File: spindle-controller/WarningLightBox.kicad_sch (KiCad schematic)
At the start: 4 parts, among them J22 GX12-4

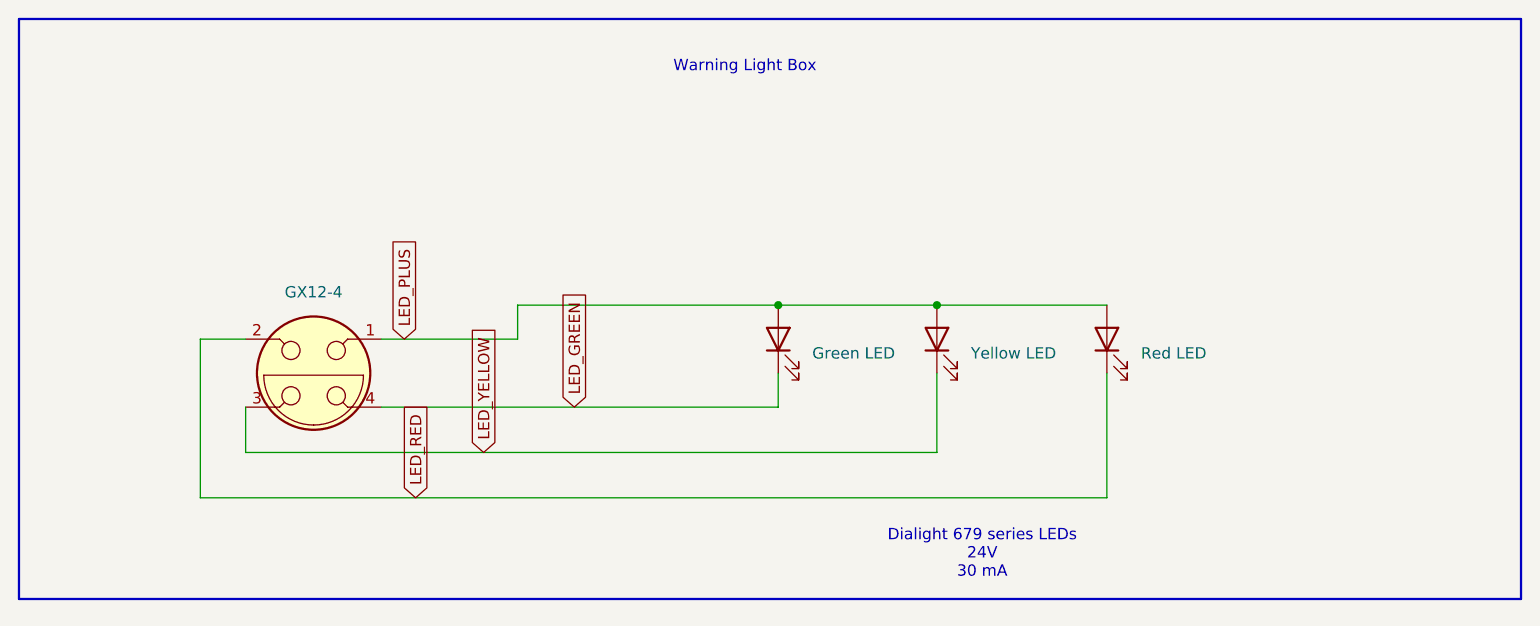
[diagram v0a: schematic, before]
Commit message: Rename project to Spindle_Controller; add VFD_DI1 spindle command path
Renamed CNC_router -> Spindle_Controller for clarity, since this
project is specifically about the spindle controller rather than the
router as a whole. Also adds the GX12-7 cable connector and VFD_DI1
wiring needed to command the spindle on, routes it through a DPDT
safety-interlock switch (SW1) shared with the warning light circuit,
fixes a DAC/ADC signal swap on VFD_VF1/VFD_FM1, and reconciles several
net labels between the root schematic and the VFD Enclosure /
TechnoCNC Controller / Warning Light Box sub-sheets.

Co-Authored-By: Claude Sonnet 5 <noreply@anthropic.com>
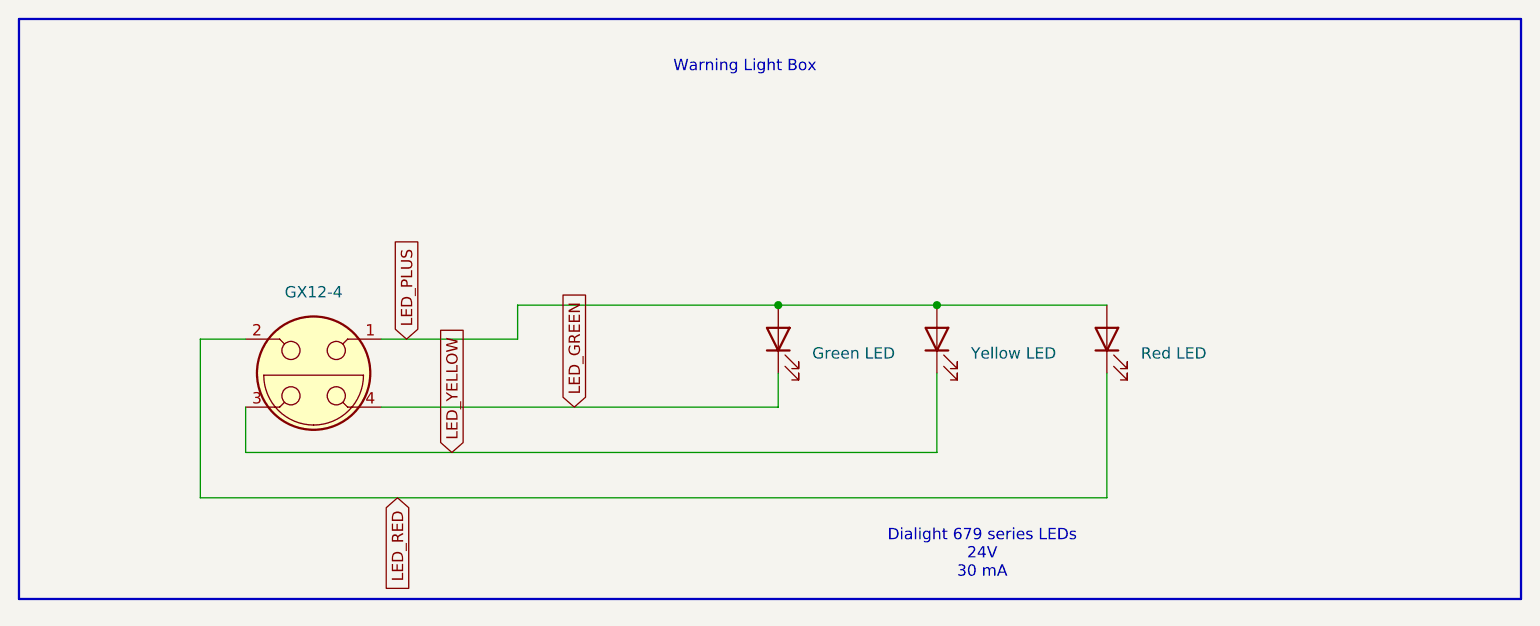
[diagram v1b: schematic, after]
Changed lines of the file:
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@@
 	(global_label "LED_YELLOW"
 		(shape input)
-		(at 78.74 68.58 90)
+		(at 75.184 68.58 90)
 		(fields_autoplaced yes)
 		(effects
@@
 		)
 		(property "Intersheetrefs" "${INTERSHEET_REFS}"
-			(at 78.74 54.1044 90)
+			(at 75.184 54.1044 90)
 			(hide yes)
 			(show_name no)
@@
 	(global_label "LED_PLUS"
 		(shape input)
-		(at 69.85 55.88 90)
+		(at 70.104 55.88 90)
 		(fields_autoplaced yes)
 		(effects
@@
 		)
 		(property "Intersheetrefs" "${INTERSHEET_REFS}"
-			(at 69.85 43.642 90)
+			(at 70.104 43.642 90)
 			(hide yes)
 			(show_name no)
@@
 	(global_label "LED_RED"
 		(shape input)
-		(at 71.12 73.66 90)
+		(at 69.088 73.66 270)
 		(fields_autoplaced yes)
 		(effects
@@
 				(size 1.27 1.27)
 			)
-			(justify left)
+			(justify right)
 		)
 		(property "Intersheetrefs" "${INTERSHEET_REFS}"
-			(at 71.12 62.5711 90)
-			(hide yes)
-			(show_name no)
-			(do_not_autoplace no)
-			(effects
-				(font
-					(size 1.27 1.27)
-				)
-				(justify left)
+			(at 69.088 84.7489 90)
+			(hide yes)
+			(show_name no)
+			(do_not_autoplace no)
+			(effects
+				(font
+					(size 1.27 1.27)
+				)
+				(justify right)
 			)
 		)
@@
 		)
 		(instances
-			(project "CNC_router"
+			(project "Spindle_Controller"
 				(path "/10c7a81d-d8e0-4023-94dc-af5199d847de/686995af-2256-4cfc-a238-558e0c36d6fd"
 					(reference "D2")
@@
 		)
 		(instances
-			(project "CNC_router"
+			(project "Spindle_Controller"
 				(path "/10c7a81d-d8e0-4023-94dc-af5199d847de/686995af-2256-4cfc-a238-558e0c36d6fd"
 					(reference "D1")
@@
 		)
 		(instances
-			(project "CNC_router"
+			(project "Spindle_Controller"
 				(path "/10c7a81d-d8e0-4023-94dc-af5199d847de/686995af-2256-4cfc-a238-558e0c36d6fd"
 					(reference "D3")
@@
 		)
 		(instances
-			(project "CNC_router"
+			(project "Spindle_Controller"
 				(path "/10c7a81d-d8e0-4023-94dc-af5199d847de/686995af-2256-4cfc-a238-558e0c36d6fd"
 					(reference "J22")
